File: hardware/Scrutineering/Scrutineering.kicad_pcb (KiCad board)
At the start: 2 copper layers, 53.5 x 55.5 mm, 17 parts, among them J1 Conn_01x04, J10 Conn_01x03, J11 Conn_01x02, J12 Conn_01x01, J13 Conn_01x01, J2 Conn_01x04, J3 Conn_01x01, J4 Conn_01x01, J5 Conn_01x03, J6 Conn_01x04, J7 Conn_01x04, J8 Conn_01x01, J9 Conn_01x01, SW1 SW_SPDT_TEMP1, SW2 SW_SPDT_TEMP2, SW3 SW_SPDT_VOLT1, SW4 SW_SPDT_VOLT2

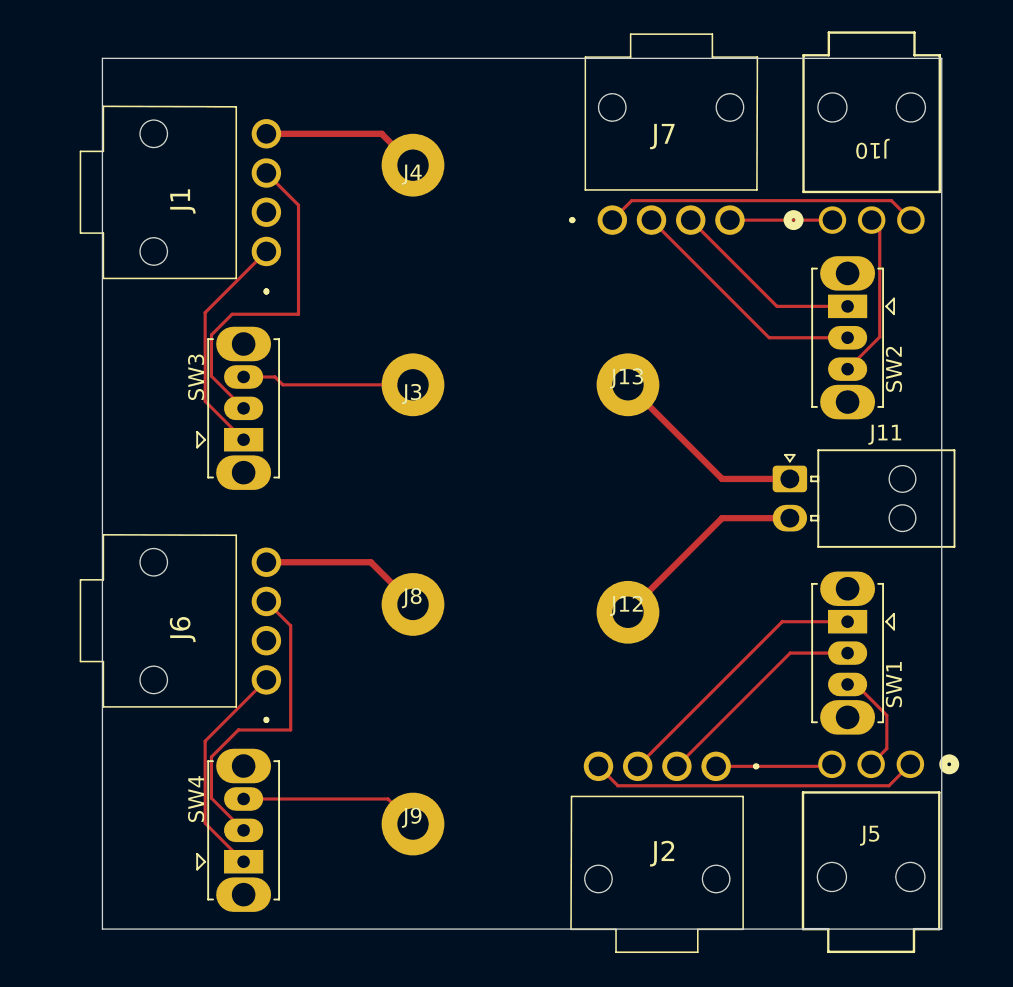
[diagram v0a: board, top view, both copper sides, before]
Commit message: updated layout
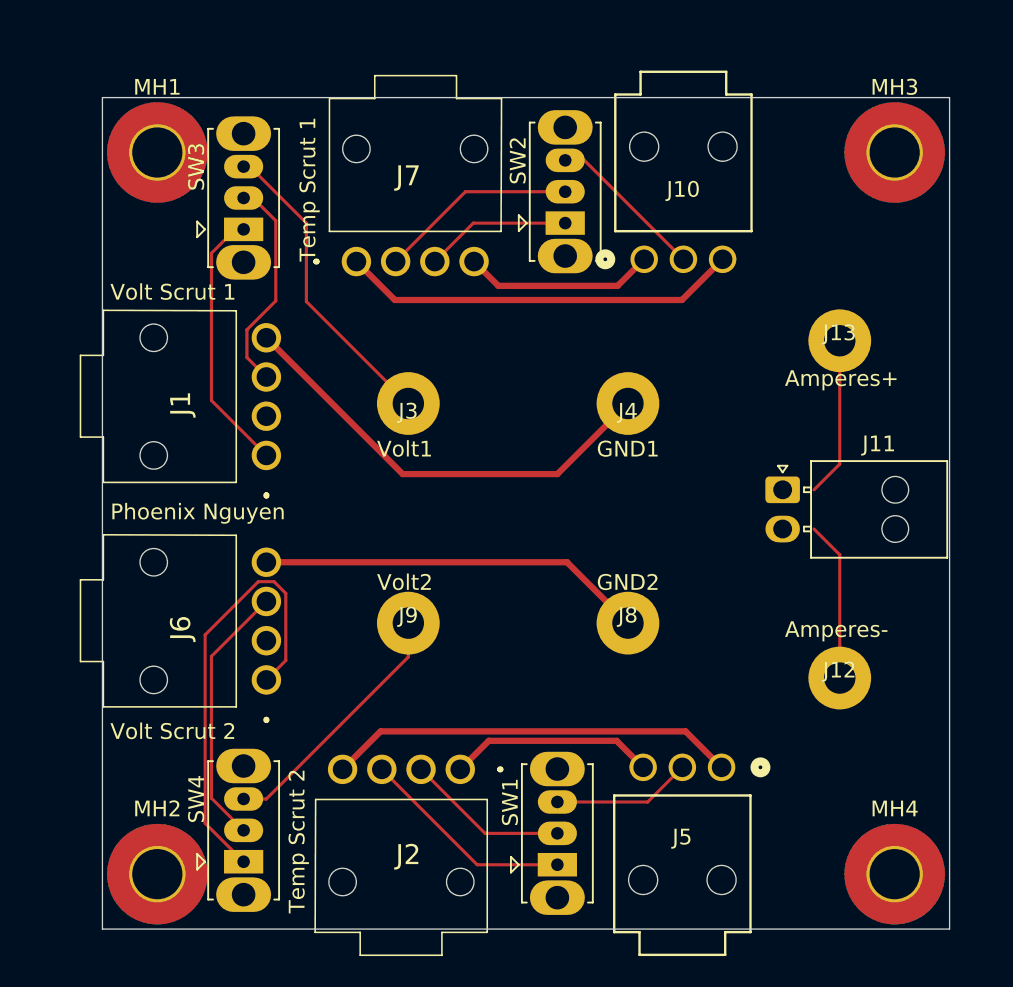
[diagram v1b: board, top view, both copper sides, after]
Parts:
- added LOGO1: Dr. Hallock, UTSVT_Logos:Hallock_Image_Small, B.Cu at (118.0, 77.7)
- added LOGO2: LHRs, UTSVT_Logos:LHRs_LOGO, F.Cu at (118.0, 77.4)
- added MH1: MountingHole_Pad, MountingHole:MountingHole_3.2mm_M3_Pad_TopBottom, F.Cu at (94.0, 55.5)
- added MH2: MountingHole_Pad, MountingHole:MountingHole_3.2mm_M3_Pad_TopBottom, F.Cu at (94.0, 101.5)
- added MH3: MountingHole_Pad, MountingHole:MountingHole_3.2mm_M3_Pad_TopBottom, F.Cu at (141.0, 55.5)
- added MH4: MountingHole_Pad, MountingHole:MountingHole_3.2mm_M3_Pad_TopBottom, F.Cu at (141.0, 101.5)
- moved SW1 24.1 mm to (119.5, 100.9), turned to 90 degrees
- moved J4 20.5 mm to (124.0, 71.5)
- moved SW2 18.8 mm to (120.0, 60.0), turned to 90 degrees
- moved J7 16.5 mm to (106.7, 62.5)
- moved J2 16.3 mm to (113.3, 94.8)
- moved J12 14.1 mm to (137.5, 89.0)
- moved J13 13.8 mm to (137.5, 67.5)
- moved J8 13.8 mm to (124.0, 85.5)
- moved SW3 13.4 mm to (99.5, 60.4)
- moved J1 13.0 mm to (101.0, 74.8)
- moved J9 12.8 mm to (110.0, 85.5)
- moved J10 12.3 mm to (125.0, 62.3)
- moved J5 12.0 mm to (130.0, 94.7)
- moved J3 1.23 mm to (110.0, 71.5)
- moved J11 0.83 mm to (133.9, 77.0)
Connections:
- net /inputTemp1 renamed /inputTemp7
- net /inputTemp2 renamed /inputTemp8
- net /inputVolt1 renamed /inputVolt7
- net /inputVolt2 renamed /inputVolt8
- net /outVolt1 renamed /voltTap7
- net /outVolt2 renamed /voltTap8
- net /rawTemp1 renamed /rawTemp7
- net /rawTemp2 renamed /rawTemp8
- net /scrutTemp1 renamed /scrutTemp7
- net /scrutTemp2 renamed /scrutTemp8
- net Net-(J1-Pin_4) renamed /GND_Seg7
- net Net-(J10-Pin_1) renamed /GNDA_8
- net Net-(J10-Pin_3) renamed /VDDA_8
- net Net-(J11-Pin_1) renamed /scrut+
- net Net-(J11-Pin_2) renamed /scrut-
- net Net-(J2-Pin_1) renamed /VDDA_7
- net Net-(J2-Pin_4) renamed /GNDA_7
- net Net-(J3-Pin_1) renamed /scrutVolt7
- net Net-(J6-Pin_4) renamed /GND_Seg8
- net Net-(J9-Pin_1) renamed /scrutVolt8
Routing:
- net /GND_Seg7: track 10.2 -> 28.5 mm
- net /GND_Seg8: track 10.5 -> 24.7 mm
- net /voltTap8: track 14.2 -> 28.4 mm
- net /scrutVolt7: track 11.0 -> 19.7 mm
- net /inputVolt7: track 21.5 -> 13.9 mm
- net /VDDA_7: track 7.43 -> 13.1 mm
- net /GNDA_8: track 6.53 -> 12.2 mm
- net /VDDA_8: track 20.1 -> 25.4 mm
- net /GNDA_7: track 21.0 -> 26.1 mm
- net /scrutVolt8: track 11.5 -> 16.4 mm
- net /rawTemp7: track 17.2 -> 13.7 mm
- net /inputTemp7: track 13.9 -> 10.4 mm
- net /inputVolt8: track 20.1 -> 16.9 mm
- net /rawTemp8: track 12.3 -> 9.33 mm
- net /inputTemp8: track 15.6 -> 12.7 mm
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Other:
- board size 53.5 x 55.5 mm -> 54 x 53 mm
- board text added: "Amperes+"
- board text added: "Amperes-"
- board text added: "GND1"
- board text added: "GND2"
- board text added: "Phoenix Nguyen"
- board text added: "Temp Scrut 1"
- board text added: "Temp Scrut 2"
- board text added: "Volt Scrut 1"
- board text added: "Volt Scrut 2"
- board text added: "Volt1"
- board text added: "Volt2"

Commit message: graphics stuff
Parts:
- moved LOGO2 0.81 mm to (118.5, 78.0)
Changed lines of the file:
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@@
 	(footprint "UTSVT_Logos:LHRs_LOGO"
 		(layer "F.Cu")
-		(at 118 77.36)
+		(at 118.5 78)
 		(property "Reference" "LOGO2"
 			(at 2.286 8.128 0)

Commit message: fixed routing
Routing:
- net /scrut-: track 10.2 -> 12.2 mm
- net /scrut+: track 10.2 -> 12.2 mm
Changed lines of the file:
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@@
 	)
 	(segment
-		(start 137.5 81.14)
-		(end 135.86 79.5)
+		(start 135.86 79.5)
+		(end 133.86 79.5)
 		(width 0.2)
 		(layer "F.Cu")
@@
 	)
 	(segment
+		(start 137.5 81.14)
+		(end 135.86 79.5)
+		(width 0.2)
+		(layer "F.Cu")
+		(net 21)
+	)
+	(segment
+		(start 135.86 77)
+		(end 133.86 77)
+		(width 0.2)
+		(layer "F.Cu")
+		(net 22)
+	)
+	(segment

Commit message: BOM and gerber (still need to find jack P/N)
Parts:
- added J14: Conn_01x02, UTSVT_Connectors:105313-2102, F.Cu at (134.8, 62.1)
- moved J13 18.2 mm to (137.2, 94.9), turned to -90 degrees
- moved J9 4.03 mm to (138.0, 71.5)
- moved J10 3.54 mm to (138.0, 85.5)
- moved MH3 2.00 mm to (143.0, 55.5)
- moved MH4 2.00 mm to (143.0, 101.5)
- moved LOGO2 1.03 mm to (117.5, 78.2)
- moved J4 0.75 mm to (105.9, 62.5)
- moved SW4 0.75 mm to (119.2, 60.0)
- moved J3 0.64 mm to (112.7, 94.8)
- moved SW3 0.64 mm to (118.9, 100.9)
- renumbered J12 to J10, J5 to J11, J10 to J12, J11 to J13, J6 to J2, J2 to J3, J7 to J4, J4 to J5, J8 to J6, J3 to J7, J9 to J8, J13 to J9, SW3 to SW1, SW4 to SW2, SW1 to SW3, SW2 to SW4
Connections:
- J1 pad 1: /voltTap7 -> /GND_Seg7
- J1 pad 2: unconnected-(J1-Pin_2-Pad2) -> /inputVolt7
- J1 pad 3: /inputVolt7 -> unconnected-(J1-Pin_3-Pad3)
- J1 pad 4: /GND_Seg7 -> /voltTap7
- J11 pad 1: /GNDA_7 -> /VDDA_7
- J11 pad 3: /VDDA_7 -> /GNDA_7
- J12 pad 1: /GNDA_8 -> /VDDA_8
- J12 pad 3: /VDDA_8 -> /GNDA_8
- J2 pad 1: /voltTap8 -> /GND_Seg8
- J2 pad 2: unconnected-(J6-Pin_2-Pad2) -> /inputVolt8
- J2 pad 3: /inputVolt8 -> unconnected-(J2-Pin_3-Pad3)
- J2 pad 4: /GND_Seg8 -> /voltTap8
- J3 pad 1: /VDDA_7 -> /GNDA_7
- J3 pad 4: /GNDA_7 -> /VDDA_7
- J4 pad 1: /VDDA_8 -> /GNDA_8
- J4 pad 4: /GNDA_8 -> /VDDA_8
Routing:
- net /scrut+: track 12.2 -> 37.1 mm
- net /scrut-: track 12.2 -> 35.4 mm
- net /GNDA_8: track 12.2 -> 27.0 mm
- net /VDDA_7: track 13.1 -> 27.1 mm
- net /VDDA_8: track 25.4 -> 12.9 mm
- net /GNDA_7: track 26.1 -> 14.0 mm
- net /voltTap7: track 17.6 -> 8.86 mm
- net /voltTap8: track 28.4 -> 23.4 mm
- net /GND_Seg7: track 28.5 -> 24.4 mm
- net /scrutVolt7: track 19.7 -> 23.5 mm
- net /inputVolt7: track 13.9 -> 17.3 mm
- net /GND_Seg8: track 24.7 -> 27.2 mm
- net /inputVolt8: track 16.9 -> 14.4 mm
- net /scrutTemp8: track 10.1 -> 10.9 mm
- net /scrutTemp7: track 8.88 -> 9.52 mm
- added copper zone on F.Cu, net (none)
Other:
- board size 54 x 53 mm -> 56 x 53 mm
- board text added: "+"
- board text added: "-"
- board text added: "Amp Scrut"
- board text added: "BPS Scrutineering September 2025"
- board text added: "GND"
- board text added: "In"
- board text added: "Out"
- board text added: "X"
- board text added: "▲ SCRUT"
- board text added: "▼ BATT"

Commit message: final
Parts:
- TEMP1: renamed from SW3; value SW_SPDT_TEMP1 -> SW_SPDT
- TEMP2: renamed from SW4; value SW_SPDT_TEMP2 -> SW_SPDT
- VOLT1: renamed from SW1; value SW_SPDT_VOLT1 -> SW_SPDT
- VOLT2: renamed from SW2; value SW_SPDT_VOLT2 -> SW_SPDT
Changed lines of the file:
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@@
 			)
 		)
+		(property "P/N" "105-2210-201"
+			(at 0 0 180)
+			(unlocked yes)
+			(layer "F.Fab")
+			(hide yes)
+			(effects
+				(font
+					(size 1 1)
+					(thickness 0.15)
+				)
+			)
+		)
 		(property ki_fp_filters "Connector*:*_1x??_*")
 		(sheetname "/")
@@
 		(descr "CuK miniature slide switch, OS series, SPDT, https://www.ckswitches.com/media/1428/os.pdf")
 		(tags "switch SPDT")
-		(property "Reference" "SW2"
+		(property "Reference" "VOLT2"
 			(at 3.99 -2.99 90)
 			(layer "F.SilkS")
@@
 			)
 		)
-		(property "Value" "SW_SPDT_VOLT2"
+		(property "Value" "SW_SPDT"
 			(at 2 3 90)
 			(layer "F.Fab")
@@
 			)
 		)
+		(property "P/N" "OS102011MS2Q"
+			(at 0 0 90)
+			(unlocked yes)
+			(layer "F.Fab")
+			(hide yes)
+			(effects
+				(font
+					(size 1 1)
+					(thickness 0.15)
+				)
+			)
+		)
 		(sheetname "/")
 		(sheetfile "Scrutineering.kicad_sch")
@@
 			)
 		)
+		(property "P/N" "105-2210-201"
+			(at 0 0 180)
+			(unlocked yes)
+			(layer "F.Fab")
+			(hide yes)
+			(effects
+				(font
+					(size 1 1)
+					(thickness 0.15)
+				)
+			)
+		)
 		(property ki_fp_filters "Connector*:*_1x??_*")
 		(sheetname "/")
@@
 			)
 		)
+		(property "P/N" "105-2210-201"
+			(at 0 0 180)
+			(unlocked yes)
+			(layer "F.Fab")
+			(hide yes)
+			(effects
+				(font
+					(size 1 1)
+					(thickness 0.15)
+				)
+			)
+		)
 		(property ki_fp_filters "Connector*:*_1x??_*")
 		(sheetname "/")
@@
 			)
 		)
+		(property "P/N" "105-2210-201"
+			(at 0 0 0)
+			(unlocked yes)
+			(layer "F.Fab")
+			(hide yes)
+			(effects
+				(font
+					(size 1 1)
+					(thickness 0.15)
+				)
+			)
+		)
 		(property ki_fp_filters "Connector*:*_1x??_*")
 		(sheetname "/")
@@
 		(descr "CuK miniature slide switch, OS series, SPDT, https://www.ckswitches.com/media/1428/os.pdf")
 		(tags "switch SPDT")
-		(property "Reference" "SW1"
+		(property "Reference" "VOLT1"
 			(at 3.99 -2.99 90)
 			(layer "F.SilkS")
@@
 			)
 		)
-		(property "Value" "SW_SPDT_VOLT1"
+		(property "Value" "SW_SPDT"
 			(at 2 3 90)
 			(layer "F.Fab")
@@
 			)
 		)
+		(property "P/N" "OS102011MS2Q"
+			(at 0 0 90)
+			(unlocked yes)
+			(layer "F.Fab")
+			(hide yes)
+			(effects
+				(font
+					(size 1 1)
+					(thickness 0.15)
+				)
+			)
+		)
 		(sheetname "/")
 		(sheetfile "Scrutineering.kicad_sch")
@@
 		(descr "CuK miniature slide switch, OS series, SPDT, https://www.ckswitches.com/media/1428/os.pdf")
 		(tags "switch SPDT")
-		(property "Reference" "SW4"
+		(property "Reference" "TEMP2"
 			(at 3.99 -2.99 90)
 			(layer "F.SilkS")
@@
 			)
 		)
-		(property "Value" "SW_SPDT_TEMP2"
+		(property "Value" "SW_SPDT"
 			(at 2 3 90)
 			(layer "F.Fab")
@@
 			)
 		)
+		(property "P/N" "OS102011MS2Q"
+			(at 0 0 90)
+			(unlocked yes)
+			(layer "F.Fab")
+			(hide yes)
+			(effects
+				(font
+					(size 1 1)
+					(thickness 0.15)
+				)
+			)
+		)
 		(sheetname "/")
 		(sheetfile "Scrutineering.kicad_sch")
@@
 			)
 		)
+		(property "P/N" "105-2210-201"
+			(at 0 0 180)
+			(unlocked yes)
+			(layer "F.Fab")
+			(hide yes)
+			(effects
+				(font
+					(size 1 1)
+					(thickness 0.15)
+				)
+			)
+		)
 		(property ki_fp_filters "Connector*:*_1x??_*")
 		(sheetname "/")
@@
 		(descr "CuK miniature slide switch, OS series, SPDT, https://www.ckswitches.com/media/1428/os.pdf")
 		(tags "switch SPDT")
-		(property "Reference" "SW3"
+		(property "Reference" "TEMP1"
 			(at 3.99 -2.99 90)
 			(layer "F.SilkS")
@@
 			)
 		)
-		(property "Value" "SW_SPDT_TEMP1"
+		(property "Value" "SW_SPDT"
 			(at 2 3 90)
 			(layer "F.Fab")
@@
 			)
 		)
+		(property "P/N" "OS102011MS2Q"
+			(at 0 0 90)
+			(unlocked yes)
+			(layer "F.Fab")
+			(hide yes)
+			(effects
+				(font
+					(size 1 1)
+					(thickness 0.15)
+				)
+			)
+		)
 		(sheetname "/")
 		(sheetfile "Scrutineering.kicad_sch")
@@
 					(thickness 0.15)
 				)
+			)
+		)
+		(property "P/N" "105-2210-201"
+			(at 0 0 0)
+			(unlocked yes)
+			(layer "F.Fab")
+			(hide yes)
+			(effects
+				(font
+					(size 1 1)
+					(thickness 0.15)
+				)

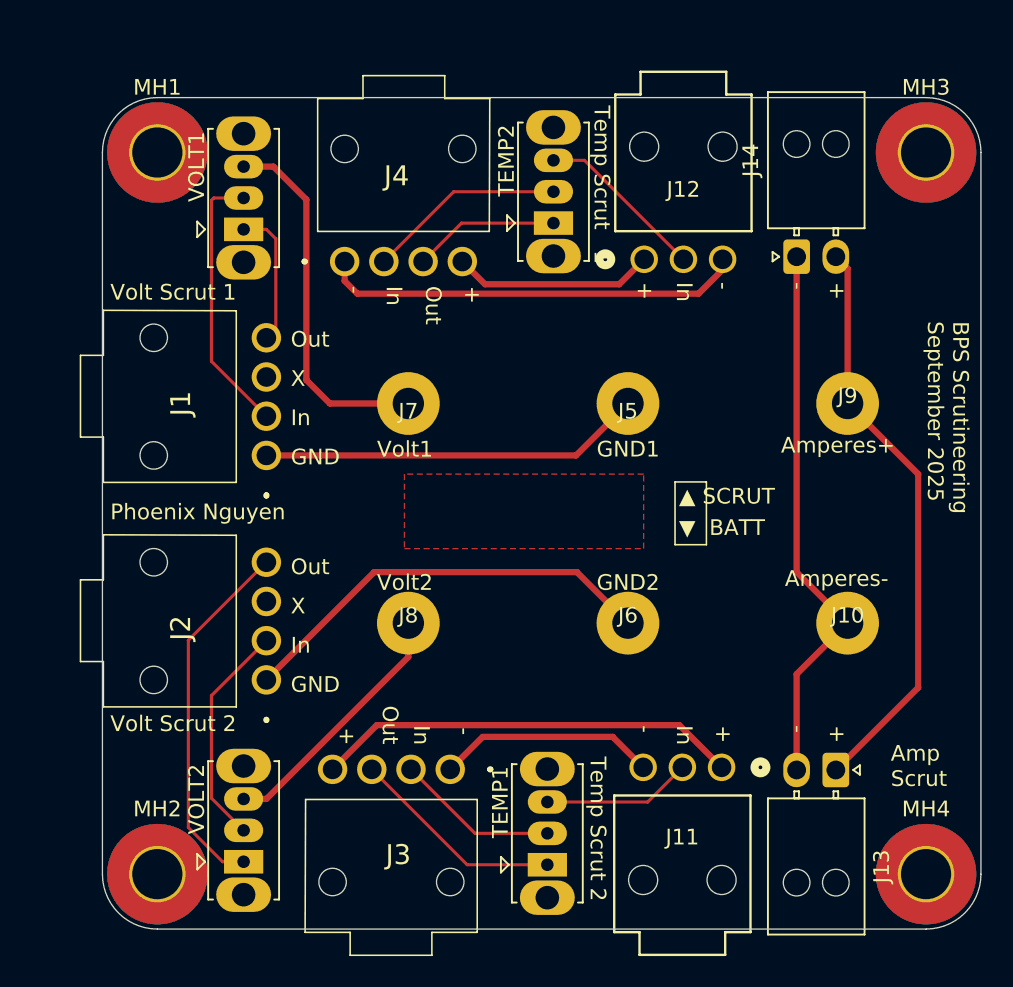
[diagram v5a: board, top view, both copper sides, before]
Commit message: BOM and gerber with changed connector
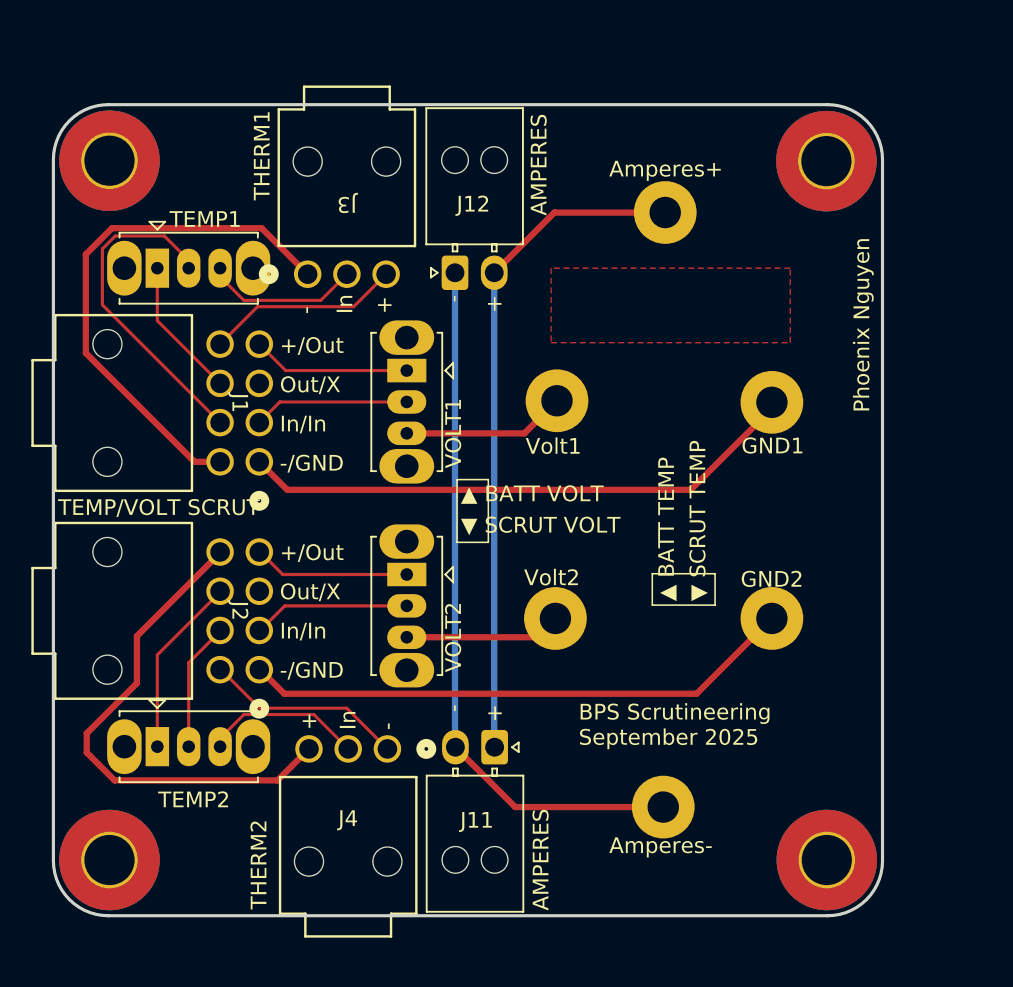
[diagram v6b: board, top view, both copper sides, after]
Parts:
- removed the J11 at (130.0, 94.7)
- removed the J12 at (125.0, 62.3)
- J1, J2: value Conn_01x04 -> Conn_02x04; footprint VoltTemp:1053132104 -> Scrutineering:nanofit_02x04
- J3, J4: value Conn_01x04 -> Conn_01x03; footprint VoltTemp:1053132104 -> VoltTemp:1053131103
- moved MH4 52.1 mm to (91.0, 100.6)
- moved MH3 52.1 mm to (91.0, 56.0)
- moved TEMP1 45.4 mm to (94.0, 62.9), turned to 0 degrees
- moved MH2 42.7 mm to (136.7, 100.6)
- moved MH1 42.7 mm to (136.7, 56.0)
- moved TEMP2 41.9 mm to (94.0, 93.4), turned to 0 degrees
- moved J3 32.8 mm to (103.6, 63.3), turned to 180 degrees
- moved J4 31.2 mm to (108.7, 93.5), turned to 0 degrees
- moved J12 21.8 mm to (113.0, 63.2)
- moved J11 21.8 mm to (115.5, 93.4)
- moved VOLT2 21.1 mm to (109.9, 82.4), turned to -90 degrees
- moved J9 16.8 mm to (126.4, 59.3)
- moved J10 16.6 mm to (126.2, 97.2)
- moved LOGO2 16.1 mm to (126.8, 65.1)
- moved VOLT1 13.8 mm to (109.9, 69.4), turned to -90 degrees
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- renumbered J13 to J11, J14 to J12
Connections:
- J3 pad 2: /inputTemp7 -> /scrutTemp7
- J3 pad 3: /rawTemp7 -> /VDDA_7
- J4 pad 2: /inputTemp8 -> /scrutTemp8
- J4 pad 3: /rawTemp8 -> /VDDA_8
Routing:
- net /VDDA_8: track 12.9 -> 32.9 mm
- net /GNDA_7: track 14.0 -> 33.8 mm
- net /VDDA_7: track 27.1 -> 12.4 mm
- net /GNDA_8: track 27.0 -> 12.8 mm
- net /voltTap8: track 23.4 -> 9.99 mm
- net /scrutVolt7: track 23.5 -> 10.4 mm
- net /GND_Seg7: track 24.4 -> 35.2 mm
- net /inputTemp7: track 10.4 -> 21.2 mm
- net /scrut-: track 35.4 -> 45.1 mm
- net /GND_Seg8: track 27.2 -> 35.3 mm
- net /inputVolt7: track 17.3 -> 9.95 mm
- net /scrutVolt8: track 16.4 -> 9.97 mm
- net /scrut+: track 37.1 -> 42.7 mm
- net /rawTemp7: track 13.7 -> 9.00 mm
- net /inputVolt8: track 14.4 -> 10.0 mm
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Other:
- board size 56 x 53 mm -> 52.8 x 51.7 mm
- board text added: "+/Out"
- board text added: "-/GND"
- board text added: "AMPERES"
- board text added: "In/In"
- board text added: "Out/X"
- board text added: "TEMP/VOLT SCRUT"
- board text added: "THERM1"
- board text added: "THERM2"
- board text added: "▲ BATT TEMP"
- board text added: "▲ BATT VOLT"
- board text added: "▼ SCRUT TEMP"
- board text added: "▼ SCRUT VOLT"
- board text removed: "Amp Scrut"
- board text removed: "GND"
- board text removed: "Out"
- board text removed: "Temp Scrut 1"
- board text removed: "Temp Scrut 2"
- board text removed: "Volt Scrut 1"
- board text removed: "Volt Scrut 2"
- board text removed: "X"
- board text removed: "▲ SCRUT"
- board text removed: "▼ BATT"
